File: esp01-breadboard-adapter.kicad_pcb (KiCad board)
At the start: 2 copper layers, 3 parts, among them P1 CONN_02X04, P2 CONN_01X04, P3 CONN_01X04

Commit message: begin 2nd layer pcb
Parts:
- added C1: C, Capacitors_SMD:C_1206, F.Cu at (137.0, 106.6)
- moved P3 3.17 mm to (140.8, 114.8)
- moved P1 1.78 mm to (133.3, 120.8)
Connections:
- P2 pad 1: RXD -> GPIO0
- P2 pad 2: GPIO0 -> RESET
- P2 pad 3: GPIO2 -> RXD
- P2 pad 4: GND -> VCC
- P3 pad 2: CH_PD -> GND
- P3 pad 3: RESET -> CH_PD
- P3 pad 4: VCC -> GPIO2
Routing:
- net GND: track 0.00 -> 10.4 mm
- net RXD: track 0.00 -> 10.3 mm
- net RESET: track 0.00 -> 10.3 mm
- net CH_PD: track 0.00 -> 10.1 mm
- net TXD: track 0.00 -> 3.48 mm
- net VCC: track 0.00 -> 3.43 mm
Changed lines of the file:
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@@
 (kicad_pcb (version 4) (host pcbnew 4.0.2-stable)
   (general
-    (links 8)
-    (no_connects 8)
+    (links 10)
+    (no_connects 4)
     (area 0 0 0 0)
     (thickness 1.6)
     (drawings 0)
-    (tracks 0)
+    (tracks 23)
     (zones 0)
-    (modules 3)
+    (modules 4)
     (nets 9)
   )
@@
     (pad_to_mask_clearance 0.2)
     (aux_axis_origin 0 0)
-    (visible_elements FFFFFF7F)
+    (visible_elements 7FFFFFFF)
     (pcbplotparams
       (layerselection 0x00030_80000001)
@@
   )
   (module Pin_Headers:Pin_Header_Straight_2x04 (layer F.Cu)
-    (at 131.572 120.65 90)
+    (at 133.35 120.777 90)
     (descr "Through hole pin header")
     (tags "pin header")
@@
     (fp_line (start -1.55 -1.55) (end 1.55 -1.55) (layer F.SilkS) (width 0.15))
     (pad 1 thru_hole rect (at 0 0) (size 2.032 1.7272) (drill 1.016) (layers *.Cu *.Mask)
+      (net 3 GPIO0))
+    (pad 2 thru_hole oval (at 0 2.54) (size 2.032 1.7272) (drill 1.016) (layers *.Cu *.Mask)
+      (net 4 RESET))
+    (pad 3 thru_hole oval (at 0 5.08) (size 2.032 1.7272) (drill 1.016) (layers *.Cu *.Mask)
       (net 1 RXD))
-    (pad 2 thru_hole oval (at 0 2.54) (size 2.032 1.7272) (drill 1.016) (layers *.Cu *.Mask)
-      (net 3 GPIO0))
-    (pad 3 thru_hole oval (at 0 5.08) (size 2.032 1.7272) (drill 1.016) (layers *.Cu *.Mask)
-      (net 5 GPIO2))
     (pad 4 thru_hole oval (at 0 7.62) (size 2.032 1.7272) (drill 1.016) (layers *.Cu *.Mask)
-      (net 7 GND))
+      (net 2 VCC))
     (model Pin_Headers.3dshapes/Pin_Header_Straight_1x04.wrl
       (at (xyz 0 -0.15 0))
@@
   )
   (module Pin_Headers:Pin_Header_Straight_1x04 (layer F.Cu)
-    (at 137.668 114.808 180)
+    (at 140.843 114.808 180)
     (descr "Through hole pin header")
     (tags "pin header")
@@
       (net 8 TXD))
     (pad 2 thru_hole oval (at 0 2.54 180) (size 2.032 1.7272) (drill 1.016) (layers *.Cu *.Mask)
+      (net 7 GND))
+    (pad 3 thru_hole oval (at 0 5.08 180) (size 2.032 1.7272) (drill 1.016) (layers *.Cu *.Mask)
       (net 6 CH_PD))
-    (pad 3 thru_hole oval (at 0 5.08 180) (size 2.032 1.7272) (drill 1.016) (layers *.Cu *.Mask)
-      (net 4 RESET))
     (pad 4 thru_hole oval (at 0 7.62 180) (size 2.032 1.7272) (drill 1.016) (layers *.Cu *.Mask)
-      (net 2 VCC))
+      (net 5 GPIO2))
     (model Pin_Headers.3dshapes/Pin_Header_Straight_1x04.wrl
       (at (xyz 0 -0.15 0))
@@
     )
   )
+  (module Capacitors_SMD:C_1206 (layer F.Cu)
+    (at 137.033 106.553)
+    (descr "Capacitor SMD 1206, reflow soldering, AVX (see smccp.pdf)")
+    (tags "capacitor 1206")
+    (attr smd)
+    (fp_text reference C1 (at 0 -2.3) (layer F.SilkS)
+      (effects (font (size 1 1) (thickness 0.15)))
+    )
+    (fp_text value C (at 0 2.3) (layer F.Fab)
+      (effects (font (size 1 1) (thickness 0.15)))
+    )
+    (fp_line (start -1.6 0.8) (end -1.6 -0.8) (layer F.Fab) (width 0.15))
+    (fp_line (start 1.6 0.8) (end -1.6 0.8) (layer F.Fab) (width 0.15))
+    (fp_line (start 1.6 -0.8) (end 1.6 0.8) (layer F.Fab) (width 0.15))
+    (fp_line (start -1.6 -0.8) (end 1.6 -0.8) (layer F.Fab) (width 0.15))
+    (fp_line (start -2.3 -1.15) (end 2.3 -1.15) (layer F.CrtYd) (width 0.05))
+    (fp_line (start -2.3 1.15) (end 2.3 1.15) (layer F.CrtYd) (width 0.05))
+    (fp_line (start -2.3 -1.15) (end -2.3 1.15) (layer F.CrtYd) (width 0.05))
+    (fp_line (start 2.3 -1.15) (end 2.3 1.15) (layer F.CrtYd) (width 0.05))
+    (fp_line (start 1 -1.025) (end -1 -1.025) (layer F.SilkS) (width 0.15))
+    (fp_line (start -1 1.025) (end 1 1.025) (layer F.SilkS) (width 0.15))
+    (pad 1 smd rect (at -1.5 0) (size 1 1.6) (layers F.Cu F.Paste F.Mask)
+      (net 2 VCC))
+    (pad 2 smd rect (at 1.5 0) (size 1 1.6) (layers F.Cu F.Paste F.Mask)
+      (net 7 GND))
+    (model Capacitors_SMD.3dshapes/C_1206.wrl
+      (at (xyz 0 0 0))
+      (scale (xyz 1 1 1))
+      (rotate (xyz 0 0 0))
+    )
+  )
+  (segment (start 133.35 120.777) (end 133.35 120.269) (width 0.25) (layer F.Cu) (net 1) (status C00000))
+  (segment (start 133.35 120.269) (end 134.62 118.999) (width 0.25) (layer F.Cu) (net 1) (status 400000))
+  (segment (start 134.62 118.999) (end 134.62 116.205) (width 0.25) (layer F.Cu) (net 1))
+  (segment (start 134.62 116.205) (end 135.255 115.57) (width 0.25) (layer F.Cu) (net 1))
+  (segment (start 135.255 115.57) (end 135.255 113.792) (width 0.25) (layer F.Cu) (net 1))
+  (segment (start 135.255 113.792) (end 133.731 112.268) (width 0.25) (layer F.Cu) (net 1) (status 800000))
+  (segment (start 133.731 112.268) (end 133.35 112.268) (width 0.25) (layer F.Cu) (net 1) (status C00000))
+  (segment (start 133.35 118.237) (end 133.35 114.808) (width 0.25) (layer F.Cu) (net 2))
+  (segment (start 135.89 118.237) (end 135.89 110.998) (width 0.25) (layer F.Cu) (net 4))
+  (segment (start 134.62 109.728) (end 133.35 109.728) (width 0.25) (layer F.Cu) (net 4))
+  (segment (start 135.89 110.998) (end 134.62 109.728) (width 0.25) (layer F.Cu) (net 4))
+  (segment (start 138.43 118.237) (end 138.43 111.125) (width 0.25) (layer F.Cu) (net 6))
+  (segment (start 138.43 111.125) (end 139.827 109.728) (width 0.25) (layer F.Cu) (net 6))
+  (segment (start 139.827 109.728) (end 140.843 109.728) (width 0.25) (layer F.Cu) (net 6))
+  (segment (start 140.97 120.777) (end 140.97 120.65) (width 0.25) (layer F.Cu) (net 7) (status C00000))
+  (segment (start 140.97 120.65) (end 139.7 119.38) (width 0.25) (layer F.Cu) (net 7) (status 400000))
+  (segment (start 139.7 119.38) (end 139.7 116.967) (width 0.25) (layer F.Cu) (net 7))
+  (segment (start 139.7 116.967) (end 139.192 116.459) (width 0.25) (layer F.Cu) (net 7))
+  (segment (start 139.192 116.459) (end 139.192 113.157) (width 0.25) (layer F.Cu) (net 7))
+  (segment (start 139.192 113.157) (end 140.081 112.268) (width 0.25) (layer F.Cu) (net 7) (status 800000))
+  (segment (start 140.081 112.268) (end 140.843 112.268) (width 0.25) (layer F.Cu) (net 7) (status C00000))
+  (segment (start 140.97 118.237) (end 140.97 114.935) (width 0.25) (layer F.Cu) (net 8))
+  (segment (start 140.97 114.935) (end 140.843 114.808) (width 0.25) (layer F.Cu) (net 8))
 )

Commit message: pcb almost finished
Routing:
- net GPIO2: track 0.00 -> 15.2 mm
- net GPIO0: track 0.00 -> 14.7 mm
- net GND: track 10.4 -> 0.00 mm
- net VCC: track 3.43 -> 0.00 mm
- added copper zone on B.Cu, net GND
- added copper zone on F.Cu, net VCC
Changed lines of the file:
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@@
-(kicad_pcb (version 4) (host pcbnew 4.0.2-stable)
+(kicad_pcb (version 4) (host pcbnew 4.0.1-stable)
   (general
     (links 10)
     (no_connects 4)
-    (area 0 0 0 0)
+    (area 122.907667 99.967 164.747334 125.816)
     (thickness 1.6)
     (drawings 0)
-    (tracks 23)
+    (tracks 27)
     (zones 0)
     (modules 4)
@@
     )
   )
-  (segment (start 133.35 120.777) (end 133.35 120.269) (width 0.25) (layer F.Cu) (net 1) (status C00000))
-  (segment (start 133.35 120.269) (end 134.62 118.999) (width 0.25) (layer F.Cu) (net 1) (status 400000))
+  (segment (start 133.35 120.777) (end 133.35 120.269) (width 0.25) (layer F.Cu) (net 1))
+  (segment (start 133.35 120.269) (end 134.62 118.999) (width 0.25) (layer F.Cu) (net 1))
   (segment (start 134.62 118.999) (end 134.62 116.205) (width 0.25) (layer F.Cu) (net 1))
   (segment (start 134.62 116.205) (end 135.255 115.57) (width 0.25) (layer F.Cu) (net 1))
   (segment (start 135.255 115.57) (end 135.255 113.792) (width 0.25) (layer F.Cu) (net 1))
-  (segment (start 135.255 113.792) (end 133.731 112.268) (width 0.25) (layer F.Cu) (net 1) (status 800000))
-  (segment (start 133.731 112.268) (end 133.35 112.268) (width 0.25) (layer F.Cu) (net 1) (status C00000))
-  (segment (start 133.35 118.237) (end 133.35 114.808) (width 0.25) (layer F.Cu) (net 2))
+  (segment (start 135.255 113.792) (end 133.731 112.268) (width 0.25) (layer F.Cu) (net 1))
+  (segment (start 133.731 112.268) (end 133.35 112.268) (width 0.25) (layer F.Cu) (net 1))
+  (segment (start 135.89 120.777) (end 135.89 120.396) (width 0.25) (layer B.Cu) (net 3) (status C00000))
+  (segment (start 135.89 120.396) (end 134.62 119.126) (width 0.25) (layer B.Cu) (net 3) (status 400000))
+  (segment (start 134.62 119.126) (end 134.62 116.586) (width 0.25) (layer B.Cu) (net 3))
+  (segment (start 134.62 116.586) (end 134.747 116.459) (width 0.25) (layer B.Cu) (net 3))
+  (segment (start 134.747 116.459) (end 134.747 108.585) (width 0.25) (layer B.Cu) (net 3))
+  (segment (start 134.747 108.585) (end 133.35 107.188) (width 0.25) (layer B.Cu) (net 3) (status 800000))
   (segment (start 135.89 118.237) (end 135.89 110.998) (width 0.25) (layer F.Cu) (net 4))
   (segment (start 134.62 109.728) (end 133.35 109.728) (width 0.25) (layer F.Cu) (net 4))
   (segment (start 135.89 110.998) (end 134.62 109.728) (width 0.25) (layer F.Cu) (net 4))
+  (segment (start 138.43 120.777) (end 138.43 120.396) (width 0.25) (layer B.Cu) (net 5) (status C00000))
+  (segment (start 138.43 120.396) (end 139.7 119.126) (width 0.25) (layer B.Cu) (net 5) (status 400000))
+  (segment (start 139.7 119.126) (end 139.7 117.094) (width 0.25) (layer B.Cu) (net 5))
+  (segment (start 139.7 117.094) (end 138.938 116.332) (width 0.25) (layer B.Cu) (net 5))
+  (segment (start 138.938 116.332) (end 138.938 109.093) (width 0.25) (layer B.Cu) (net 5))
+  (segment (start 138.938 109.093) (end 140.843 107.188) (width 0.25) (layer B.Cu) (net 5) (status 800000))
   (segment (start 138.43 118.237) (end 138.43 111.125) (width 0.25) (layer F.Cu) (net 6))
   (segment (start 138.43 111.125) (end 139.827 109.728) (width 0.25) (layer F.Cu) (net 6))
   (segment (start 139.827 109.728) (end 140.843 109.728) (width 0.25) (layer F.Cu) (net 6))
-  (segment (start 140.97 120.777) (end 140.97 120.65) (width 0.25) (layer F.Cu) (net 7) (status C00000))
-  (segment (start 140.97 120.65) (end 139.7 119.38) (width 0.25) (layer F.Cu) (net 7) (status 400000))
-  (segment (start 139.7 119.38) (end 139.7 116.967) (width 0.25) (layer F.Cu) (net 7))
-  (segment (start 139.7 116.967) (end 139.192 116.459) (width 0.25) (layer F.Cu) (net 7))
-  (segment (start 139.192 116.459) (end 139.192 113.157) (width 0.25) (layer F.Cu) (net 7))
-  (segment (start 139.192 113.157) (end 140.081 112.268) (width 0.25) (layer F.Cu) (net 7) (status 800000))
-  (segment (start 140.081 112.268) (end 140.843 112.268) (width 0.25) (layer F.Cu) (net 7) (status C00000))
   (segment (start 140.97 118.237) (end 140.97 114.935) (width 0.25) (layer F.Cu) (net 8))
   (segment (start 140.97 114.935) (end 140.843 114.808) (width 0.25) (layer F.Cu) (net 8))
+  (zone (net 2) (net_name VCC) (layer F.Cu) (hatch edge 0.508)
+    (connect_pads (clearance 0.508))
+    (min_thickness 0.254)
+    (fill (arc_segments 16) (thermal_gap 0.508) (thermal_bridge_width 0.508))
+    (polygon
+      (pts
+        (xy 131.318 105.283) (xy 142.748 105.283) (xy 142.875 122.682) (xy 131.445 122.682) (xy 131.318 105.41)
+      )
+    )
+  )
+  (zone (net 7) (net_name GND) (layer B.Cu) (hatch edge 0.508)
+    (connect_pads (clearance 0.508))
+    (min_thickness 0.254)
+    (fill (arc_segments 16) (thermal_gap 0.508) (thermal_bridge_width 0.508))
+    (polygon
+      (pts
+        (xy 131.191 105.283) (xy 142.748 105.283) (xy 142.875 122.682) (xy 131.445 122.682) (xy 131.191 105.283)
+      )
+    )
+  )
 )

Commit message: pcb faces ok
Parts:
- P2, P3: moved to B.Cu
- turned P2 to 180 degrees
- turned P3 to 0 degrees
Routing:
- net GPIO2: track 15.2 -> 0.38 mm
- net GPIO0: track 14.7 -> 0.38 mm
- net CH_PD: track 10.1 -> 0.00 mm
- net RESET: track 10.3 -> 0.32 mm
- net RXD: track 10.3 -> 1.27 mm
- net TXD: track 3.48 -> 0.18 mm
- net GND: track 0.00 -> 1.96 mm, vias 0 -> 1
- removed copper zone on B.Cu, net GND
- removed copper zone on F.Cu, net VCC

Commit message: pcb finished
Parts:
- C1: value C -> 100u
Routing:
- net GND: track 1.96 -> 18.4 mm
- net GPIO0: track 0.38 -> 16.4 mm, vias 0 -> 1
- net VCC: track 0.00 -> 15.8 mm, vias 0 -> 1
- net GPIO2: track 0.38 -> 16.1 mm, vias 0 -> 1
- net CH_PD: track 0.00 -> 10.7 mm, vias 0 -> 1
- net RESET: track 0.32 -> 10.8 mm, vias 0 -> 1
- net RXD: track 1.27 -> 10.9 mm, vias 0 -> 1
- net TXD: track 0.18 -> 4.50 mm, vias 0 -> 1
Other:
- board outline added: 14.6 x 17.4 mm
- board text added: "CH_PD"
- board text added: "GND"
- board text added: "GPIO0"
- board text added: "GPIO2"
- board text added: "RESET"
- board text added: "RXD"
- board text added: "TXD"
- board text added: "VCC"

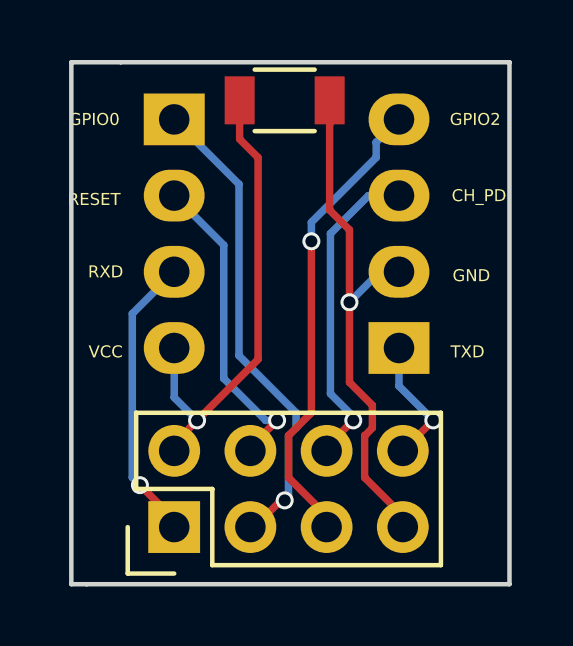
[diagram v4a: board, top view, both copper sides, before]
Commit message: pcb finished, added copper pour on both layers
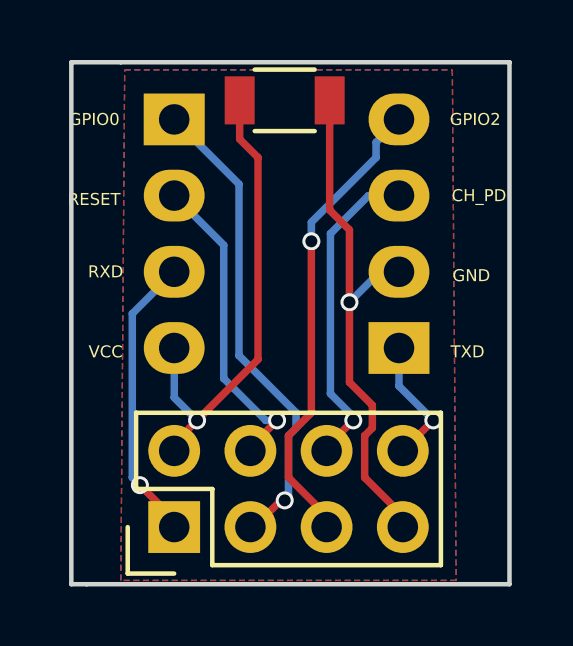
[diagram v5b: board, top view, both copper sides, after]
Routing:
- added copper zone on B.Cu, net GND
- added copper zone on F.Cu, net VCC
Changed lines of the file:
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@@
     (last_trace_width 0.25)
     (trace_clearance 0.2)
-    (zone_clearance 0.508)
+    (zone_clearance 0.2)
     (zone_45_only no)
     (trace_min 0.2)
@@
     (descr "Through hole pin header")
     (tags "pin header")
-    (fp_text reference P1 (at -8.001 -1.27 180) (layer F.SilkS) hide
+    (fp_text reference P1 (at -5.334 -2.032 180) (layer F.SilkS) hide
       (effects (font (size 1 1) (thickness 0.15)))
     )
-    (fp_text value CONN_02X04 (at -6.477 2.54 180) (layer F.Fab) hide
+    (fp_text value CONN_02X04 (at -3.81 1.905 180) (layer F.Fab) hide
       (effects (font (size 1 1) (thickness 0.15)))
     )
@@
     (tags "capacitor 1206")
     (attr smd)
-    (fp_text reference C1 (at -1.397 -5.715) (layer F.SilkS) hide
+    (fp_text reference C1 (at -1.651 -3.937) (layer F.SilkS) hide
       (effects (font (size 1 1) (thickness 0.15)))
     )
-    (fp_text value 100u (at -0.508 -4.318) (layer F.Fab) hide
+    (fp_text value 100u (at -0.635 -2.794) (layer F.Fab) hide
       (effects (font (size 1 1) (thickness 0.15)))
     )
@@
   (via (at 141.986 117.221) (size 0.6) (drill 0.4) (layers F.Cu B.Cu) (net 8))
   (segment (start 140.97 114.935) (end 140.843 114.808) (width 0.25) (layer F.Cu) (net 8))
+  (zone (net 2) (net_name VCC) (layer F.Cu) (hatch edge 0.508)
+    (connect_pads (clearance 0.2))
+    (min_thickness 0.254)
+    (fill yes (arc_segments 16) (thermal_gap 0.508) (thermal_bridge_width 0.508))
+    (polygon
+      (pts
+        (xy 131.699 105.537) (xy 142.621 105.537) (xy 142.748 122.555) (xy 131.572 122.555) (xy 131.699 105.537)
+      )
+    )
+  )
+  (zone (net 7) (net_name GND) (layer B.Cu) (hatch edge 0.508)
+    (connect_pads (clearance 0.2))
+    (min_thickness 0.254)
+    (fill yes (arc_segments 16) (thermal_gap 0.508) (thermal_bridge_width 0.508))
+    (polygon
+      (pts
+        (xy 131.699 105.537) (xy 142.621 105.537) (xy 142.748 122.555) (xy 131.572 122.555) (xy 131.699 105.537)
+      )
+    )
+  )
 )

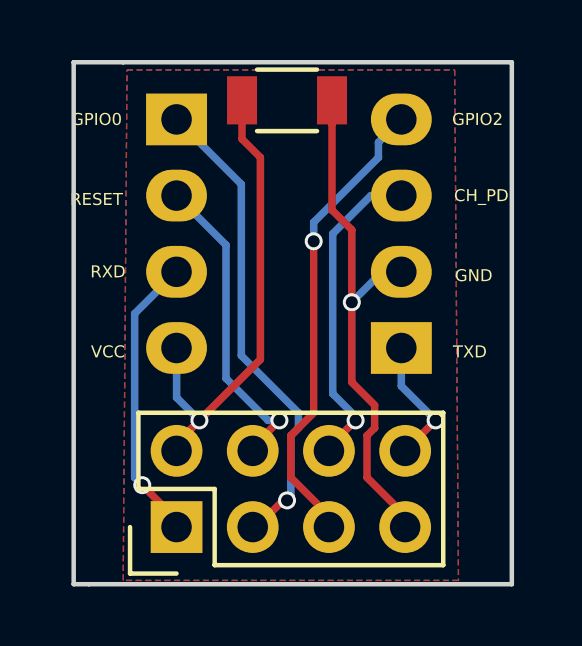
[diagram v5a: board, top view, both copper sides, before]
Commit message: edited edge cuts
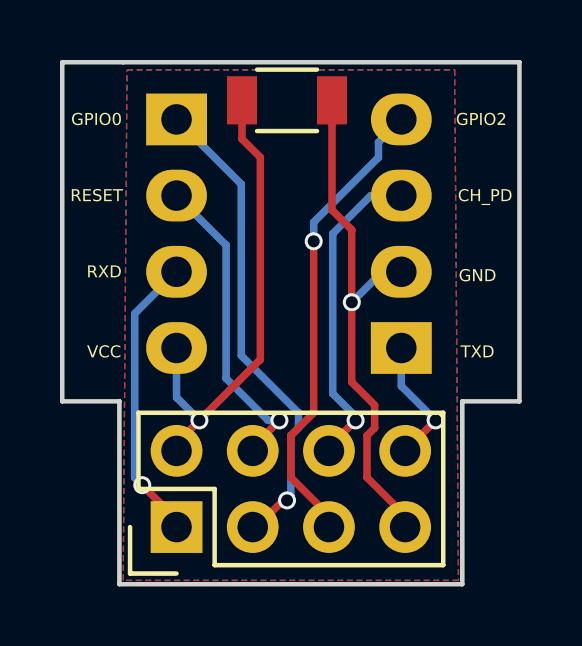
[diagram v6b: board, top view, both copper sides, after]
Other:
- board size 14.6 x 17.4 mm -> 15.2 x 17.4 mm
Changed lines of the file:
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@@
     (links 10)
     (no_connects 0)
-    (area 129.845999 105.207999 144.601001 122.757001)
+    (area 129.464999 105.207999 144.855001 122.757001)
     (thickness 1.6)
-    (drawings 14)
+    (drawings 17)
     (tracks 78)
     (zones 0)
@@
     )
   )
-  (gr_line (start 129.921 105.283) (end 131.572 105.283) (angle 90) (layer Edge.Cuts) (width 0.15))
-  (gr_line (start 129.921 122.682) (end 129.921 105.283) (angle 90) (layer Edge.Cuts) (width 0.15))
-  (gr_line (start 130.429 122.682) (end 129.921 122.682) (angle 90) (layer Edge.Cuts) (width 0.15))
-  (gr_line (start 144.526 122.682) (end 130.429 122.682) (angle 90) (layer Edge.Cuts) (width 0.15))
-  (gr_line (start 144.526 105.283) (end 144.526 122.682) (angle 90) (layer Edge.Cuts) (width 0.15))
-  (gr_line (start 131.572 105.283) (end 144.526 105.283) (angle 90) (layer Edge.Cuts) (width 0.15))
+  (gr_line (start 129.54 105.283) (end 131.572 105.283) (angle 90) (layer Edge.Cuts) (width 0.15))
+  (gr_line (start 129.54 116.586) (end 129.54 105.283) (angle 90) (layer Edge.Cuts) (width 0.15))
+  (gr_line (start 131.445 116.586) (end 129.54 116.586) (angle 90) (layer Edge.Cuts) (width 0.15))
+  (gr_line (start 131.445 122.682) (end 131.445 116.586) (angle 90) (layer Edge.Cuts) (width 0.15))
+  (gr_line (start 142.875 122.682) (end 131.445 122.682) (angle 90) (layer Edge.Cuts) (width 0.15))
+  (gr_line (start 142.875 116.586) (end 142.875 122.682) (angle 90) (layer Edge.Cuts) (width 0.15))
+  (gr_text RESET (at 130.683 109.728) (layer F.SilkS)
+    (effects (font (size 0.4 0.4) (thickness 0.075)))
+  )
+  (gr_line (start 144.78 116.586) (end 142.875 116.586) (angle 90) (layer Edge.Cuts) (width 0.15))
+  (gr_line (start 144.78 105.283) (end 144.78 116.586) (angle 90) (layer Edge.Cuts) (width 0.15))
+  (gr_line (start 131.572 105.283) (end 144.78 105.283) (angle 90) (layer Edge.Cuts) (width 0.15))
   (gr_text "GPIO0\n" (at 130.683 107.188) (layer F.SilkS)
     (effects (font (size 0.4 0.4) (thickness 0.075)))
   )
-  (gr_text RESET (at 130.683 109.855) (layer F.SilkS)
-    (effects (font (size 0.4 0.4) (thickness 0.075)))
-  )
-  (gr_text "RXD\n" (at 131.064 112.268) (layer F.SilkS)
-    (effects (font (size 0.4 0.4) (thickness 0.075)))
-  )
-  (gr_text "VCC\n" (at 131.064 114.935) (layer F.SilkS)
-    (effects (font (size 0.4 0.4) (thickness 0.075)))
-  )
-  (gr_text TXD (at 143.129 114.935) (layer F.SilkS)
-    (effects (font (size 0.4 0.4) (thickness 0.075)))
-  )
-  (gr_text GND (at 143.256 112.395) (layer F.SilkS)
-    (effects (font (size 0.4 0.4) (thickness 0.075)))
-  )
-  (gr_text CH_PD (at 143.51 109.728) (layer F.SilkS)
-    (effects (font (size 0.4 0.4) (thickness 0.075)))
-  )
-  (gr_text "GPIO2\n" (at 143.383 107.188) (layer F.SilkS)
-    (effects (font (size 0.4 0.4) (thickness 0.075)))
-  )
+  (gr_text "RXD\n" (at 130.937 112.268) (layer F.SilkS)
+    (effects (font (size 0.4 0.4) (thickness 0.075)))
+  )
+  (gr_text "VCC\n" (at 130.937 114.935) (layer F.SilkS)
+    (effects (font (size 0.4 0.4) (thickness 0.075)))
+  )
+  (gr_text TXD (at 143.383 114.935) (layer F.SilkS)
+    (effects (font (size 0.4 0.4) (thickness 0.075)))
+  )
+  (gr_text GND (at 143.383 112.395) (layer F.SilkS)
+    (effects (font (size 0.4 0.4) (thickness 0.075)))
+  )
+  (gr_text CH_PD (at 143.637 109.728) (layer F.SilkS)
+    (effects (font (size 0.4 0.4) (thickness 0.075)))
+  )
+  (gr_text "GPIO2\n" (at 143.51 107.188) (layer F.SilkS)
+    (effects (font (size 0.4 0.4) (thickness 0.075)))
+  )

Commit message: pcb complete
pcb complete with signed bottom sikscreen
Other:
- board text added: "github.com/fu0x11"
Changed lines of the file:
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@@
     (area 129.464999 105.207999 144.855001 122.757001)
     (thickness 1.6)
-    (drawings 17)
+    (drawings 18)
     (tracks 78)
     (zones 0)
@@
   (page A4)
   (layers
-    (0 F.Cu signal)
-    (31 B.Cu signal)
+    (0 F.Cu signal hide)
+    (31 B.Cu signal hide)
     (32 B.Adhes user)
     (33 F.Adhes user)
@@
     )
   )
+  (gr_text github.com/fu0x11 (at 138.557 112.522 90) (layer B.SilkS)
+    (effects (font (size 0.5 0.5) (thickness 0.125)))
+  )
   (gr_line (start 129.54 105.283) (end 131.572 105.283) (angle 90) (layer Edge.Cuts) (width 0.15))
